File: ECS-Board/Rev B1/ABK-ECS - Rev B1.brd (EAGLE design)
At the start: 100 x 80 mm, 247 parts, among them J10 22-05-7068-06, J11 FTSH-105-01-L-DV-NOPASTE, J2 USB-B-S-RA, J21 FTSH-103-01-L-DV-NOPASTE, J4 MSTBA2, J5 22-05-7068-06, J6 22-05-7028-02, J7 22-05-7068-06, J8 22-05-7068-06, J9 22-05-7028-02, K1 G6K-2G-Y, SW1 B3FS-1015, SW2 B3FS-1015, T1 EXMACHINA-LOGO-NAME, T10 MMBT2222AL, T11 MMBT2222AL, T12 IRLML5103TRPBF, T13 IRLML5103TRPBF, T14 IRLML5103TRPBF, T15 IRLML5103TRPBF, T16 MMBT2222AL, T17 MMBT2222AL, T18 MMBT2222AL, T19 MMBT2222AL, T2 IRLML5103TRPBF, T20 MMBT2907ALT3, T3 MMBT2222AL, T4 IRLML5103TRPBF, T5 IRLML5103TRPBF, T6 IRLML5103TRPBF, T7 IRLML5103TRPBF, T8 MMBT2222AL, T9 MMBT2222AL, U1 AT24C512C-SSHM-B, U2 LPC1768FBD100, U3 LT3686HDDPBF, U4 LT3686HDDPBF, U6 CD4050BD, U7 CD4050BD, X1 FC-135, X2 ASE-12, X3 3000

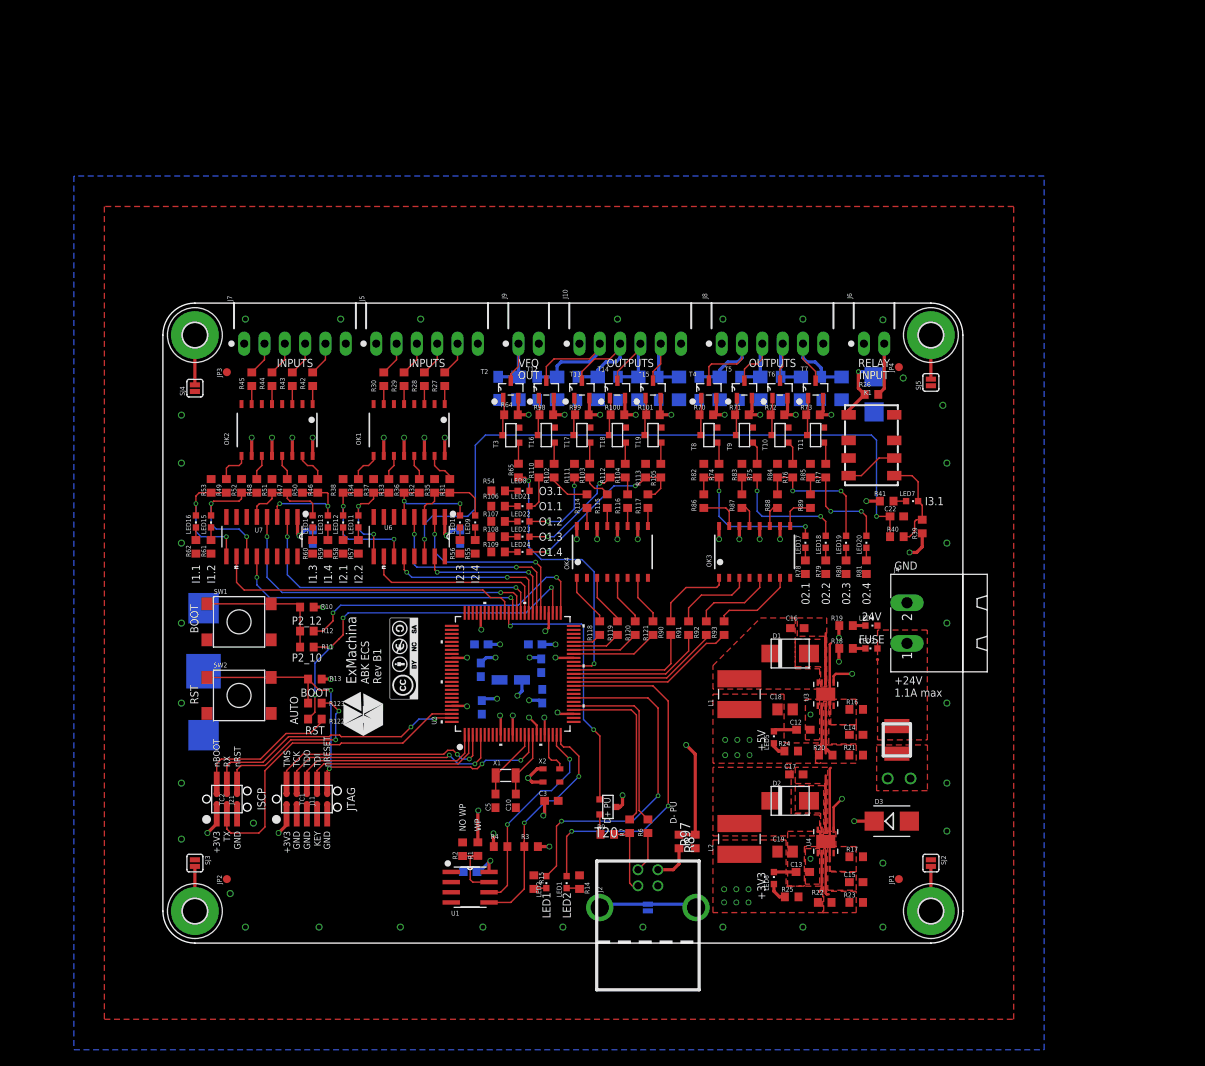
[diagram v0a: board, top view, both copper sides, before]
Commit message: Place and route ethernet interface
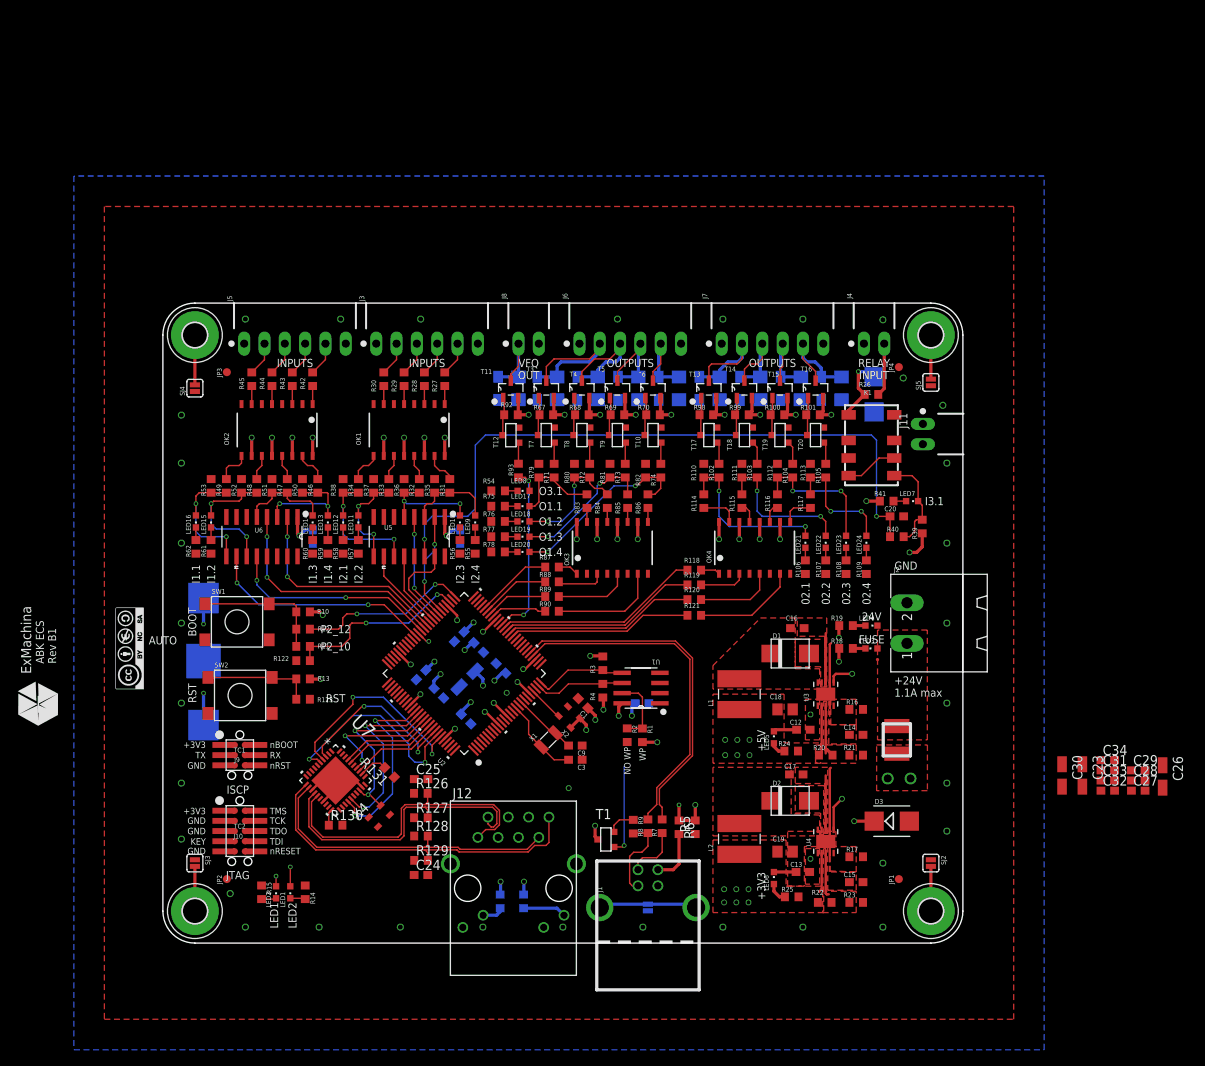
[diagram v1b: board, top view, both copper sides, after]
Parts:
- removed D14: 1N4148WS, diode:SOD323-W
- removed J21: FTSH-103-01-L-DV-NOPASTE, con-samtec:FTSH-103-01-L-DV-NOPASTE
- added C20, C21: 0.1uF, rcl:C0603
- added C25, C27, C28, C29, C31, C32, C33, C34: 100nF, rcl:C0603
- added C26, C30: 10uF, rcl:CT3216
- added D4: STPS3L40UF, diode:SMB
- added J1: USB-B-S-RA, con-multicomp:USB-B-S-RA
- added J12: RB1-125BAG1A, con-wiznet:WIZNET_RB1-125BAG1A
- added J3: 22-05-7068-06, con-molex:7395-06
- added R124, R125: 220, rcl:R0603
- added R126, R127, R128, R129: 49.9, rcl:R0603
- added R130: 4K7, rcl:R0603
- added R131: 2K2, rcl:R0603
- added U5: CD4050BD, ti:SOIC127P600X175-16N
- added X4: ASE_50, crystal:ASE
- C1: value 10uF -> 0.1uF; device rcl:CT3216 -> rcl:C0603
- C10, C5: value 18pF -> 0.1uF
- C23: value 0.1uF -> 4.7uF; device rcl:C0603 -> rcl:CT3216
- C24: value 0.1uF -> 100nF
- C3, C9: value 0.1uF -> 18pF
- C4: value 0.1uF -> 10uF; device rcl:C0603 -> rcl:CT3216
- D5: value STPS3L40UF -> 1N4148WS; device diode:SMB -> diode:SOD323-W
- J10: value 22-05-7068-06 -> FTSH-105-01-L-DV-NOPASTE; device con-molex:7395-06 -> con-samtec:FTSH-105-01-L-DV-NOPASTE
- J11: value FTSH-105-01-L-DV-NOPASTE -> 22-05-7028-02; device con-samtec:FTSH-105-01-L-DV-NOPASTE -> con-molex:7395-02
- J2: value USB-B-S-RA -> MSTBA2; device con-multicomp:USB-B-S-RA -> con-phoenix-508:MSTBA2
- J4: value MSTBA2 -> 22-05-7028-02; device con-phoenix-508:MSTBA2 -> con-molex:7395-02
- J6: value 22-05-7028-02 -> 22-05-7068-06; device con-molex:7395-02 -> con-molex:7395-06
- J8: value 22-05-7068-06 -> 22-05-7028-02; device con-molex:7395-06 -> con-molex:7395-02
- J9: value 22-05-7028-02 -> FTSH-103-01-L-DV-NOPASTE; device con-molex:7395-02 -> con-samtec:FTSH-103-01-L-DV-NOPASTE
- R5: value 1K -> 39K; device rcl:R1206 -> rcl:R0603
- R6: value 33 -> 24K
- R64: value 10K -> 1K; device rcl:R0603 -> rcl:R1206
- R65: value 100 -> 1K; device rcl:R0603 -> rcl:R1206
- R67, R68, R69: value 1K -> 10K; device rcl:R1206 -> rcl:R0603
- R71, R72, R73: value 10K -> 1K
- R75, R76, R77: value 1K -> 1K5
- R79, R80, R81: value 1K5 -> 4K7
- R8: value 24K -> 33
- R83, R84, R85: value 4K7 -> 100
- R87, R88, R89: value 100 -> 330
- R91: value 330 -> 1K; device rcl:R0603 -> rcl:R1206
- R92: value 330 -> 10K
- R93: value 330 -> 100
- R97: value 39K -> 1K; device rcl:R0603 -> rcl:R1206
- T1: value EXMACHINA-LOGO-NAME -> MMBT2907ALT3; device exmachina:EXM-LOGO-BASELINE -> transistor:SOT−23
- T11, T16, T3: value MMBT2222AL -> IRLML5103TRPBF; device transistor:SOT−23 -> International_Rectifier_By_element14_Batch_1:SOT95P240X112-3N
- T12, T7: value IRLML5103TRPBF -> MMBT2222AL; device International_Rectifier_By_element14_Batch_1:SOT95P240X112-3N -> transistor:SOT−23
- T2: value IRLML5103TRPBF -> EXMACHINA-LOGO-NAME; device International_Rectifier_By_element14_Batch_1:SOT95P240X112-3N -> exmachina:EXM-LOGO-BASELINE
- T20: value MMBT2907ALT3 -> MMBT2222AL
- TC1: value TC2050-IDC-NL -> TC2030-IDC-NL; device TagConnect:TC2050-IDC-NL -> TagConnect:TC2030-IDC-NL
- TC2: value TC2030-IDC-NL -> TC2050-IDC-NL; device TagConnect:TC2030-IDC-NL -> TagConnect:TC2050-IDC-NL
- U7: value CD4050BD -> DP83848JSQ/NOPB; device ti:SOIC127P600X175-16N -> textas:SQA40B
- moved C23 100.7 mm to (114.9, 21.0), flipped to the top
- moved J11 89.5 mm to (95.0, 63.6), turned to 90 degrees
- moved J10 78.1 mm to (9.62, 14.0), turned to 270 degrees
- moved T2 71.0 mm to (-15.6, 29.8)
- moved J9 62.8 mm to (9.62, 23.5), turned to 270 degrees
- moved J7 59.7 mm to (76.2, 74.9)
- moved R97 59.5 mm to (84.8, 69.3), flipped to the bottom
- moved R5 54.9 mm to (66.5, 14.5), flipped to the top
- moved C22 54.6 mm to (37.2, 50.8), flipped to the bottom, turned to 270 degrees
- moved T20 53.2 mm to (81.6, 63.5), turned to 270 degrees
- moved J2 51.7 mm to (98.1, 40.0), turned to 90 degrees
- moved R109 46.1 mm to (87.9, 47.0), turned to 270 degrees
- moved R108 43.7 mm to (85.4, 47.0), turned to 270 degrees
- moved LED20 42.9 mm to (45.1, 48.9), turned to 90 degrees
- moved LED24 42.9 mm to (87.9, 50.2), turned to 180 degrees
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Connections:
- removed net N$75 (its old number): LED17.A, R74.1, R82.1, R86.1
- removed net N$76 (its old number): OK3.15, R86.2
- removed net N$79 (its old number): LED18.A, R75.1, R83.1, R87.1
- removed net N$80 (its old number): OK3.13, R87.2
- removed net N$83 (its old number): LED19.A, R76.1, R84.1, R88.1
- removed net N$86 (its old number): LED20.A, R77.1, R85.1, R89.1
- removed net N$87 (its old number): OK3.11, R88.2
- removed net N$88 (its old number): OK3.9, R89.2
- removed net N$89 (its old number): OK3.1, R90.1
- removed net N$91 (its old number): OK3.3, R91.1
- removed net N$92 (its old number): OK3.7, R93.1
- removed net N$93 (its old number): OK3.5, R92.1
- removed net N$94 (its old number): LED17.C, R78.1
- removed net N$95 (its old number): LED18.C, R79.1
- removed net N$96 (its old number): LED19.C, R80.1
- removed net N$97 (its old number): LED20.C, R81.1
- new net AGND: J12.S1, J12.S2
- new net ETH_CRS: U2.92, U7.33
- new net ETH_MDC: U2.87, U7.25
- new net ETH_MDIO: U2.86, U7.24
- new net ETH_RST: U7.23
- new net ETH_RXD_0: U2.91, U7.36
- new net ETH_RXD_1: U2.90, U7.37
- new net ETH_RX_ER: U2.89, U7.34
- new net ETH_RX_N: J12.R8, R129.2, U7.11
- new net ETH_RX_P: J12.R7, R128.2, U7.12
- new net ETH_TXD_0: U2.95, U7.4
- new net ETH_TXD_1: U2.94, U7.5
- new net ETH_TXD_EN: U2.93, U7.3
- new net ETH_TX_N: J12.R2, R127.2, U7.14
- new net ETH_TX_P: J12.R1, R126.2, U7.15
- new net ETH_X1: U2.88, U7.28, X4.3
- new net L1_1: J12.L2, U7.22
- new net L1_2: J12.L4, U7.21
- new net MII_MODE: R131.2, U7.32
- new net N$113: J12.L1, R124.1
- new net N$115: J12.L3, R125.1
- new net N$116: R130.1, U7.20
- new net N$31: LED17.A, R71.1, R79.1, R83.1
- new net N$33: OK3.15, R83.2
- new net N$34: LED18.A, R72.1, R80.1, R84.1
- new net N$35: OK3.13, R84.2
- new net N$36: LED19.A, R73.1, R81.1, R85.1
- new net N$37: LED20.A, R74.1, R82.1, R86.1
- new net N$38: OK3.11, R85.2
- new net N$39: OK3.9, R86.2
- new net N$40: OK3.1, R87.1
- new net N$42: OK3.3, R88.1
- new net N$43: OK3.7, R90.1
- new net N$46: OK3.5, R89.1
- new net N$66: LED17.C, R75.1
- new net N$67: LED18.C, R76.1
- new net N$68: LED19.C, R77.1
- new net N$69: LED20.C, R78.1
- new net PFBOUT: C26.+, C27.1, C28.1, C29.1, U7.16, U7.19, U7.30
- net !ISP_BOOT: now also J9.2, TC1.2; no longer J21.2, TC2.2
- net !ISP_RST: now also J9.6, TC1.6; no longer J21.6, TC2.6
- net !RESET: now also J10.10, TC2.10; no longer J11.10, TC1.10
- net +24V: now also J3.1, J4.1, R67.2, R68.2, R69.2, R92.2, T11.2, T16.2, T3.2; no longer J10.1, J8.1, R64.2, R71.2, R72.2, R73.2, T12.2, T2.2, T7.2
- net +3V3: now also C1.1, C10.1, C21.1, C22.1, C23.+, C25.1, C30.+, C31.1, C32.1, C33.1, C34.1, C4.+, C5.1, J10.1, J12.R3, J9.1, R124.2, R125.2, R126.1, R127.1, R128.1, R129.1, R131.1, T1.3, U5.1, U7.18, U7.26, X4.1, X4.4; no longer C1.+, C23.1, C3.1, C4.1, C9.1, J11.1, J21.1, T20.3
- net +5V: now also J11.1
- net GND: now also C1.2, C20.2, C21.2, C23.-, C25.2, C26.-, C27.2, C28.2, C29.2, C30.-, C31.2, C32.2, C33.2, C34.2, C4.-, D4.A, J1.4, J10.3, J10.5, J10.7, J10.9, J11.2, J12.R4, J12.R5, J12.R6, J2.2, J3.6, J6.6, J8.2, J9.5, R130.2, R64.1, R65.1, R75.2, R76.2, R77.2, R91.1, T12.2, T20.2, T7.2, TC2.3, TC2.7, TC2.9, U5.8, U7.13, U7.17, U7.29, U7.40, U7.41, X4.2; no longer C1.-, C23.2, C4.2, D14.A, J10.6, J11.3, J11.5, J11.7, J11.9, J2.4, J21.5, J4.2, J8.6, J9.2, R67.1, R68.1, R69.1, R83.2, R84.2, R85.2, T11.2, T16.2, T3.2, TC1.3, TC1.7, TC1.9, U7.8
- net INPUT1.1: now also U6.9; no longer U7.9
- net INPUT1.1_MCU: now also U6.10; no longer U7.10
- net INPUT1.2: now also U6.11; no longer U7.11
- net INPUT1.2_MCU: now also U6.12; no longer U7.12
- net INPUT1.3: now also U6.5; no longer U7.5
- net INPUT1.3_MCU: now also U6.4; no longer U7.4
- net INPUT1.4: now also U6.3; no longer U7.3
- net INPUT1.4_MCU: now also U6.2; no longer U7.2
- net INPUT2.1: now also U5.11; no longer U6.11
- net INPUT2.1_MCU: now also U5.12; no longer U6.12
- net INPUT2.2: now also U5.9; no longer U6.9
- net INPUT2.2_MCU: now also U5.10; no longer U6.10
- net INPUT2.3: now also U5.5; no longer U6.5
- net INPUT2.3_MCU: now also U5.4; no longer U6.4
- net INPUT2.4: now also U5.3; no longer U6.3
- net INPUT2.4_MCU: now also U5.2; no longer U6.2
- net INPUT3.1: now also C20.1, U5.14; no longer C22.1, U6.14
- net INPUT3.1_MCU: now also U5.15; no longer U6.15
- net ISP_RXDO: now also J9.4, TC1.4; no longer J21.4, TC2.4
- net ISP_TXDO: now also J9.3, TC1.3; no longer J21.3, TC2.3
- net JTAG_TCK: now also J10.4, TC2.4; no longer J11.4, TC1.4
- net JTAG_TDI: now also J10.8, TC2.8; no longer J11.8, TC1.8
- net JTAG_TDO: now also J10.6, TC2.6; no longer J11.6, TC1.6
- net JTAG_TMS: now also J10.2, TC2.2; no longer J11.2, TC1.2
- net MOTOR_VFQ: now also D9.C, J8.1, R91.2, T11.3; no longer D6.C, J9.1, R68.2, T2.3
- net N$1: now also J1.3, R8.1; no longer J2.3, R7.1
- net N$102: now also J5.4; no longer J7.4
- net N$105: now also J5.3; no longer J7.3
- net N$112: now also J5.2; no longer J7.2
- net N$114: now also J1.1, R6.2; no longer J2.1, R8.2
- net N$17: now also R102.2, T17.1; no longer R74.2, T8.1
- net N$18: now also R98.1, T13.1, T17.3; no longer R70.1, T4.1, T8.3
- net N$19: now also R103.2, T18.1; no longer R75.2, T9.1
- net N$2: now also J1.2, R7.1; no longer J2.2, R6.1
- net N$20: now also R99.1, T14.1, T18.3; no longer R71.1, T5.1, T9.3
- net N$21: now also R104.2, T19.1; no longer R76.2, T10.1
- net N$22: now also R100.1, T15.1, T19.3; no longer R72.1, T10.3, T6.1
- net N$23: now also R105.2, T20.1; no longer R77.2, T11.1
- net N$24: now also R101.1, T16.1, T20.3; no longer R73.1, T11.3, T7.1
- net N$25: now also R93.1, T12.1; no longer R65.1, T3.1
- net N$26: now also R92.1, T11.1, T12.3; no longer R64.1, T2.1, T3.3
- net N$28: now also D4.C; no longer D5.C
- net N$30: now also T1.2; no longer T20.2
- net N$32: now also J4.2; no longer J6.2
- net N$52: now also J3.2; no longer J5.2
- net N$53: now also J3.3; no longer J5.3
- net N$54: now also J3.4; no longer J5.4
- net N$55: now also J3.5; no longer J5.5
- net N$70: now also J1.SHL, J1.SHL1; no longer J2.SHL, J2.SHL1
- net N$71: now also R67.1, T3.1, T7.3; no longer R98.1, T12.1, T16.3
- net N$72: now also R68.1, T4.1, T8.3; no longer R99.1, T13.1, T17.3
- net N$77: now also R69.1, T5.1, T9.3; no longer R100.1, T14.1, T18.3
- net N$78: now also R70.1, T10.3, T6.1; no longer R101.1, T15.1, T19.3
- net N$82: now also J5.5; no longer J7.5
- net N$84: now also R71.2, T7.1; no longer R102.2, T16.1
- net N$85: now also R72.2, T8.1; no longer R103.2, T17.1
- net N$98: now also R73.2, T9.1; no longer R104.2, T18.1
- net N$99: now also R74.2, T10.1; no longer R105.2, T19.1
- net OUTPUT1.1: now also D5.C, J6.2, R63.2, T3.3; no longer D11.C, J10.2, R96.2, T12.3
- net OUTPUT1.1_MCU: now also R87.2; no longer R118.2
- net OUTPUT1.2: now also D6.C, J6.3, R64.2, T4.3; no longer D12.C, J10.3, R95.2, T13.3
- net OUTPUT1.2_MCU: now also R88.2; no longer R119.2
- net OUTPUT1.3: now also D7.C, J6.4, R65.2, T5.3; no longer D13.C, J10.4, R94.2, T14.3
- net OUTPUT1.3_MCU: now also R89.2; no longer R120.2
- net OUTPUT1.4: now also D8.C, J6.5, R66.2, T6.3; no longer D14.C, J10.5, R69.2, T15.3
- net OUTPUT1.4_MCU: now also R90.2; no longer R121.2
- net OUTPUT2.1: now also D10.C, J7.2, R94.2, T13.3; no longer D7.C, J8.2, R5.2, T4.3
- net OUTPUT2.1_MCU: now also R118.2; no longer R90.2
- net OUTPUT2.2: now also D11.C, J7.3, R95.2, T14.3; no longer D8.C, J8.3, R63.2, T5.3
- net OUTPUT2.2_MCU: now also R119.2; no longer R91.2
- net OUTPUT2.3: now also D12.C, J7.4, R96.2, T15.3; no longer D9.C, J8.4, R66.2, T6.3
- net OUTPUT2.3_MCU: now also R120.2; no longer R92.2
- net OUTPUT2.4: now also D13.C, J7.5, R97.2, T16.3; no longer D10.C, J8.5, R67.2, T7.3
- net OUTPUT2.4_MCU: now also R121.2; no longer R93.2
- net OUTPUT3.2_MCU: now also R93.2; no longer R65.2
- net RTCX1: now also C3.1; no longer C5.1
- net RTCX2: now also C9.1; no longer C10.1
- net USB_CONNECT: now also T1.1; no longer T20.1
- net USB_D_N: now also R7.2; no longer R6.2
- net USB_D_P: now also R8.2; no longer R7.2
- net USB_V_BUS: now also R5.2, R6.1; no longer R8.1, R97.2
- net VIN: now also J2.1; no longer J4.1
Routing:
- net VBAT+: track 2.56 -> 62.2 mm, vias 1 -> 3
- net !RESET: track 61.9 -> 13.6 mm, vias 4 -> 0
- net ETH_RX_N: track 0.00 -> 44.1 mm
- net ISP_TXDO: track 43.3 -> 0.00 mm
- net ONBOARD_LED2: track 45.0 -> 2.43 mm, vias 2 -> 1
- net ONBOARD_LED1: track 43.1 -> 1.27 mm, vias 2 -> 1
- net ETH_RX_P: track 0.00 -> 39.0 mm
- net ETH_TX_P: track 0.00 -> 38.7 mm
- net ETH_TX_N: track 0.00 -> 37.8 mm
- net ISP_RXDO: track 34.2 -> 0.00 mm, vias 2 -> 0
- net JTAG_TMS: track 30.5 -> 0.00 mm, vias 2 -> 0
- net JTAG_TCK: track 30.4 -> 0.00 mm, vias 2 -> 0
- net ETH_TXD_0: track 0.00 -> 26.3 mm, vias 0 -> 2
- net ETH_TXD_1: track 0.00 -> 25.9 mm, vias 0 -> 2
- net JTAG_TDO: track 25.8 -> 0.00 mm
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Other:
- board text removed: "D+ PU"
- board text removed: "D- PU"

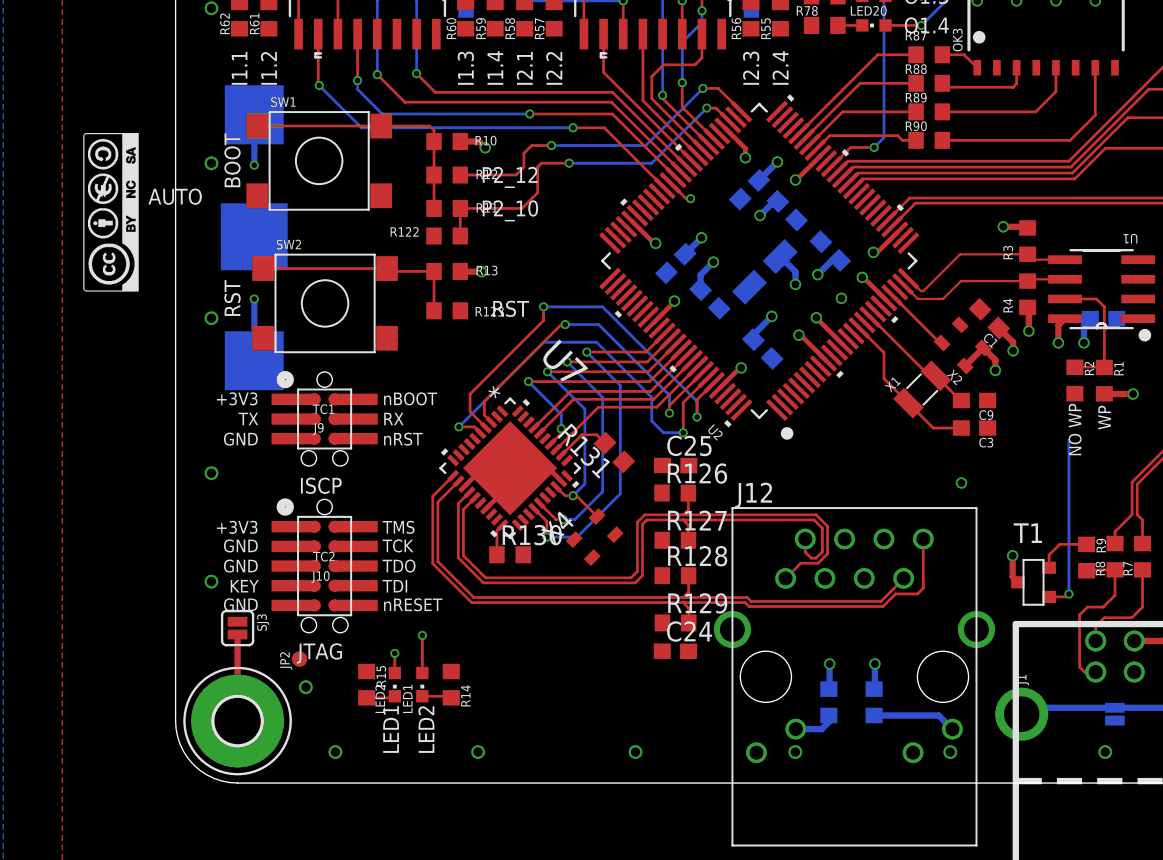
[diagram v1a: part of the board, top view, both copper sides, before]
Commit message: Route JTAG, ISCP and LED On board
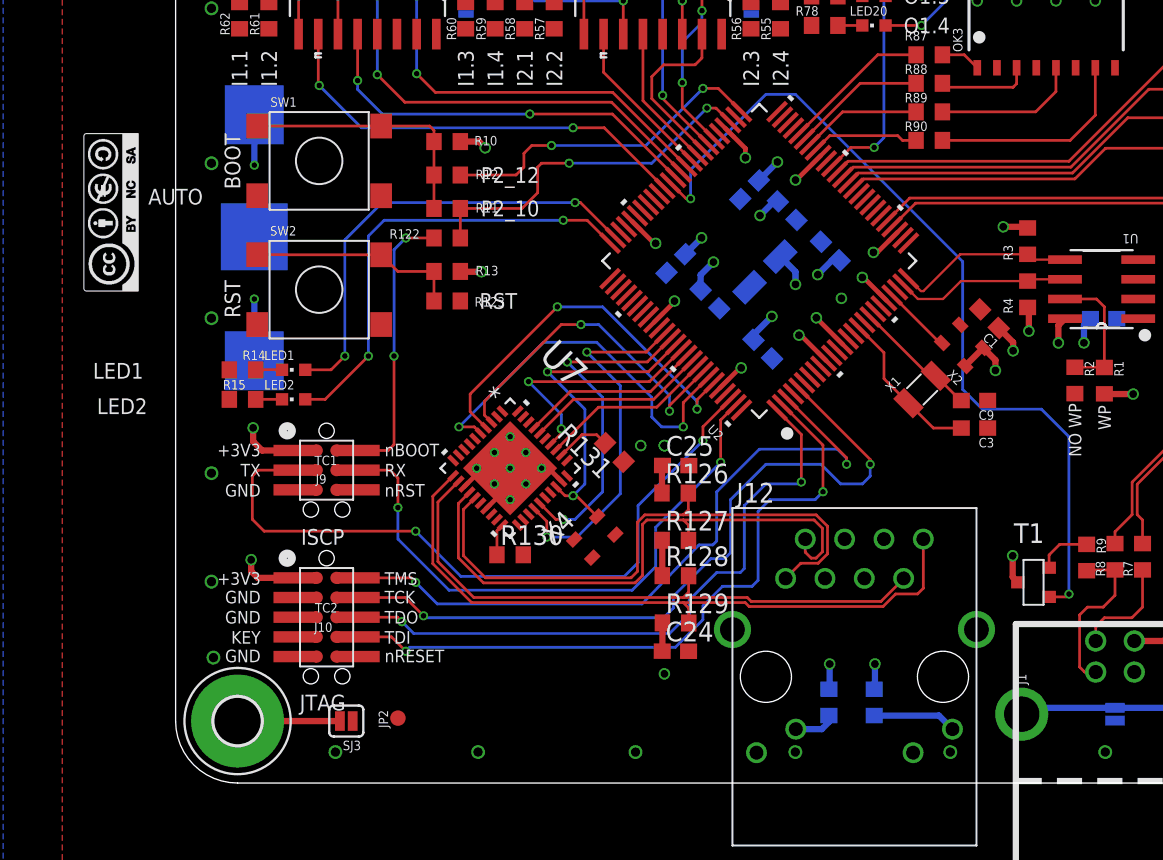
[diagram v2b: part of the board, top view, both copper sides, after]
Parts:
- moved R14 24.4 mm to (4.32, 26.7), turned to 180 degrees
- moved LED1 22.0 mm to (7.62, 26.7), turned to 90 degrees
- moved R15 20.1 mm to (4.32, 24.8), turned to 180 degrees
- moved LED2 19.5 mm to (7.62, 24.8), turned to 90 degrees
- moved SJ3 9.23 mm to (11.0, 4.00), turned to 180 degrees
- moved JP2 7.41 mm to (14.3, 4.19)
- moved J10 3.30 mm to (9.74, 10.7)
- moved J9 3.30 mm to (9.74, 20.2)
- moved TC1 3.30 mm to (9.74, 20.2)
- moved TC2 3.30 mm to (9.74, 10.7)
- moved SW2 0.97 mm to (9.27, 31.8)
- moved R123 0.63 mm to (17.5, 31.1)
- moved R122 0.13 mm to (17.5, 35.2)
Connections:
- net ONBOARD_LED1: now also U2.75
- net ONBOARD_LED2: now also U2.74
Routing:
- net JTAG_TCK: track 0.00 -> 49.9 mm, vias 0 -> 2
- net ISP_TXDO: track 0.00 -> 46.9 mm, vias 0 -> 2
- net JTAG_TMS: track 0.00 -> 46.1 mm, vias 0 -> 2
- net JTAG_TDI: track 0.00 -> 45.9 mm, vias 0 -> 2
- net JTAG_TDO: track 0.00 -> 42.7 mm, vias 0 -> 2
- net USB_CONNECT: track 13.0 -> 55.5 mm
- net ISP_RXDO: track 0.00 -> 39.4 mm, vias 0 -> 2
- net ONBOARD_LED1: track 1.27 -> 29.6 mm, vias 1 -> 2
- net ONBOARD_LED2: track 2.43 -> 29.8 mm, vias 1 -> 2
- net !ISP_BOOT: track 0.00 -> 19.3 mm, vias 0 -> 2
- net +3V3: track 66.7 -> 83.1 mm, vias 36 -> 41
- net ETH_TXD_0: track 26.3 -> 24.8 mm
- net !RESET: track 13.6 -> 15.2 mm
- net !ISP_RST: track 0.00 -> 1.40 mm
- net 2: track 5.59 -> 6.60 mm
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
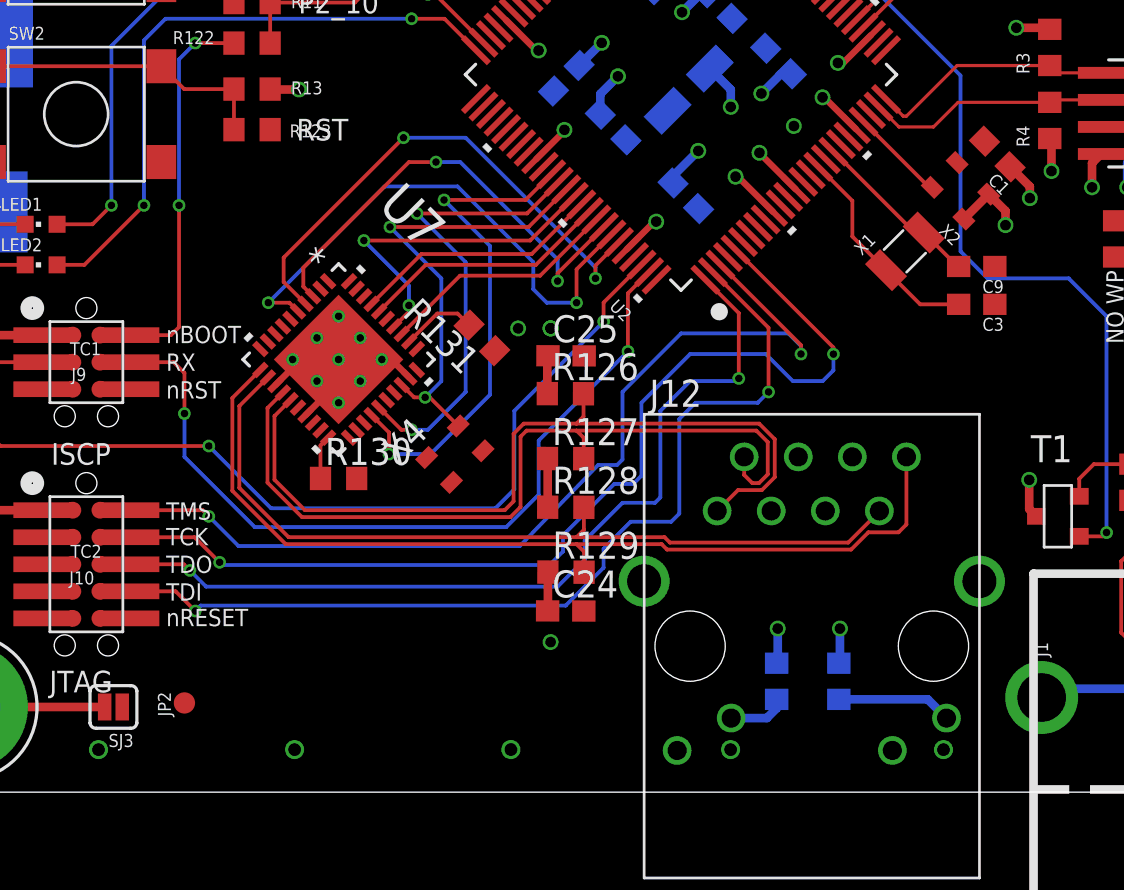
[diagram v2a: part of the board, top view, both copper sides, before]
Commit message: Route ethernet LED and Reset signal
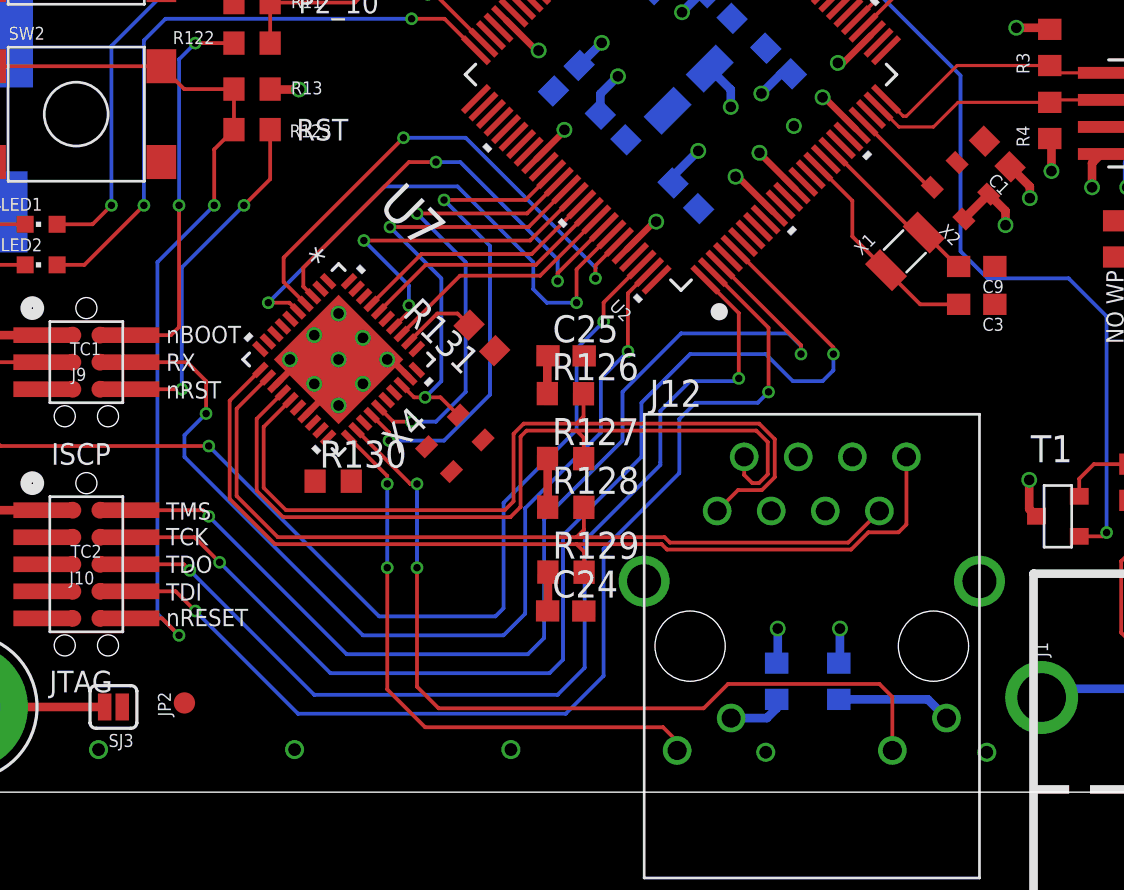
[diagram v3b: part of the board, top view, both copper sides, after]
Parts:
- moved X4 0.51 mm to (27.1, 16.4)
- moved R130 0.28 mm to (21.3, 14.6)
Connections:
- net ONBOARD_LED1: no longer U2.32
- net ONBOARD_LED2: no longer U2.35
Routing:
- net L1_1: track 0.00 -> 39.4 mm, vias 0 -> 2
- net !RESET: track 15.2 -> 43.5 mm, vias 0 -> 2
- net L1_2: track 0.00 -> 27.6 mm, vias 0 -> 2
- net !ISP_RST: track 1.40 -> 17.8 mm, vias 0 -> 2
- net ISP_RXDO: track 39.4 -> 47.7 mm
- net ISP_TXDO: track 46.9 -> 54.1 mm
- net JTAG_TMS: track 46.1 -> 53.0 mm
- net JTAG_TCK: track 49.9 -> 56.5 mm
- net JTAG_TDO: track 42.7 -> 49.0 mm
- net JTAG_TDI: track 45.9 -> 51.7 mm
- net N$116: track 2.06 -> 0.00 mm
- net ETH_TX_P: track 38.7 -> 39.6 mm
- net ETH_TX_N: track 37.8 -> 38.7 mm
- net ETH_MDIO: track 23.6 -> 22.7 mm
- net +3V3: vias 41 -> 37
